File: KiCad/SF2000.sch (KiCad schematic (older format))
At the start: 71 parts, among them J1 Conn_2Rows-86Pins_even_odd, J2 Conn_01x02, J7 Conn_02x01, U1 LM1117-3.3, U19 74LVC1G57GV, U2 ABLIC S-1132B43-M5T1U, U3 TLV75533PDBVR, U4 SN74CBT16211, U5 SN74CBT16211, U6 SN74CBT3244PW, U7 SN74LVC16245ADGGR

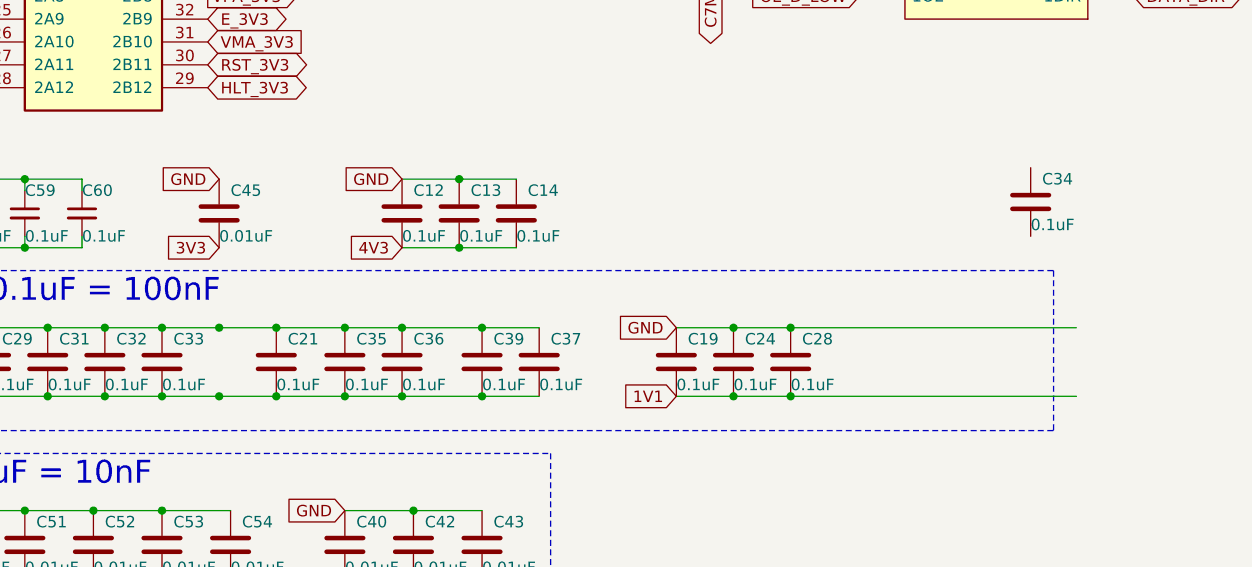
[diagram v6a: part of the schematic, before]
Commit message: Update C34,C35,C39 to 1206 4.7uF size and move to be used in RP2354A power circuit. Add a 33 Ohm series resistor on VREG_AVDD and use C34 for decoupling of the same.
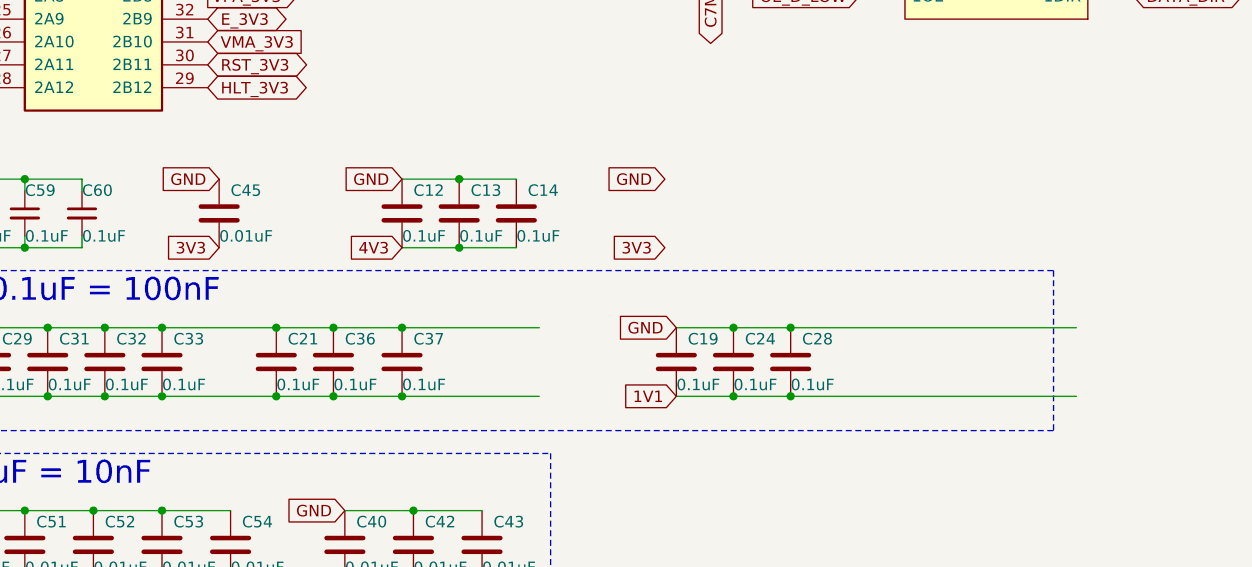
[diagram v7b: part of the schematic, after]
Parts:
- removed C34: 0.1uF, Capacitor_SMD:C_0805_2012Metric_Pad1.18x1.45mm_HandSolder, symbol Device:C
- removed C35, C39: 0.1uF, Capacitor_SMD:C_0805_2012Metric_Pad1.15x1.40mm_HandSolder, symbol Device:C
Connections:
- wire segments 135 -> 131
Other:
- moved on the sheet: C36, C37
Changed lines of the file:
@@
-$EndComp
-$Comp
-L Device:C C35
-U 1 1 62559B16
-P 6000 6150
-F 0 "C35" H 6050 6250 50  0000 L CNN
-F 1 "0.1uF" H 6000 6050 50  0000 L CNN
-F 2 "Capacitor_SMD:C_0805_2012Metric_Pad1.15x1.40mm_HandSolder" H 6038 6000 50  0001 C CNN
-F 3 "~" H 6000 6150 50  0001 C CNN
-	1    6000 6150
-	1    0    0    -1
 $EndComp
 $Comp
@@
 $EndComp
 $Comp
-L Device:C C39
-U 1 1 622B5AAE
-P 6600 6150
-F 0 "C39" H 6650 6250 50  0000 L CNN
-F 1 "0.1uF" H 6600 6050 50  0000 L CNN
-F 2 "Capacitor_SMD:C_0805_2012Metric_Pad1.15x1.40mm_HandSolder" H 6638 6000 50  0001 C CNN
-F 3 "~" H 6600 6150 50  0001 C CNN
-	1    6600 6150
-	1    0    0    -1
-$EndComp
-$Comp
 L Connector_Generic:Conn_02x01 J?
 U 1 1 62359ABC
@@
 $EndComp
 $Comp
-L Device:C C34
-U 1 1 68166D11
-P 9000 5450
-F 0 "C34" H 9050 5550 50  0000 L CNN
-F 1 "0.1uF" H 9000 5350 50  0000 L CNN
-F 2 "Capacitor_SMD:C_0805_2012Metric_Pad1.18x1.45mm_HandSolder" H 9038 5300 50  0001 C CNN
-F 3 "~" H 9000 5450 50  0001 C CNN
-	1    9000 5450
-	1    0    0    -1
-$EndComp
-$Comp
 L Device:C C33
 U 1 1 681A6453
@@
 L Device:C C37
 U 1 1 623F7CFB
-P 6850 6150
-F 0 "C37" H 6900 6250 50  0000 L CNN
-F 1 "0.1uF" H 6850 6050 50  0000 L CNN
-F 2 "Capacitor_SMD:C_0805_2012Metric_Pad1.15x1.40mm_HandSolder" H 6888 6000 50  0001 C CNN
-F 3 "~" H 6850 6150 50  0001 C CNN
-	1    6850 6150
+P 6250 6150
+F 0 "C37" H 6300 6250 50  0000 L CNN
+F 1 "0.1uF" H 6250 6050 50  0000 L CNN
+F 2 "Capacitor_SMD:C_0805_2012Metric_Pad1.15x1.40mm_HandSolder" H 6288 6000 50  0001 C CNN
+F 3 "~" H 6250 6150 50  0001 C CNN
+	1    6250 6150
 	1    0    0    -1
 $EndComp
@@
 L Device:C C36
 U 1 1 623F86B0
-P 6250 6150
-F 0 "C36" H 6300 6250 50  0000 L CNN
-F 1 "0.1uF" H 6250 6050 50  0000 L CNN
-F 2 "Capacitor_SMD:C_0805_2012Metric_Pad1.15x1.40mm_HandSolder" H 6288 6000 50  0001 C CNN
-F 3 "~" H 6250 6150 50  0001 C CNN
-	1    6250 6150
+P 5950 6150
+F 0 "C36" H 6000 6250 50  0000 L CNN
+F 1 "0.1uF" H 5950 6050 50  0000 L CNN
+F 2 "Capacitor_SMD:C_0805_2012Metric_Pad1.15x1.40mm_HandSolder" H 5988 6000 50  0001 C CNN
+F 3 "~" H 5950 6150 50  0001 C CNN
+	1    5950 6150
 	1    0    0    -1
 $EndComp
@@
 Wire Wire Line
 	2200 6050 2200 6000
-Wire Wire Line
-	5450 6000 5700 6000
-Connection ~ 5450 6000
 Connection ~ 5700 6000
-Wire Wire Line
-	5700 6000 6000 6000
-Wire Wire Line
-	5450 6300 5700 6300
-Connection ~ 5450 6300
 Connection ~ 5700 6300
-Wire Wire Line
-	5700 6300 6000 6300
 Wire Wire Line
 	7450 6000 7700 6000
@@
 Connection ~ 3950 6000
 Connection ~ 3950 6300
-Connection ~ 6000 6000
-Connection ~ 6000 6300
 Wire Wire Line
 	3950 6000 4200 6000
@@
 Wire Wire Line
 	4450 6300 4700 6300
-Wire Wire Line
-	6000 6000 6250 6000
-Wire Wire Line
-	6000 6300 6250 6300
 Connection ~ 6250 6000
-Wire Wire Line
-	6250 6000 6600 6000
 Connection ~ 6250 6300
-Wire Wire Line
-	6250 6300 6600 6300
 Connection ~ 4700 6000
 Connection ~ 4700 6300
 Wire Wire Line
-	6850 6000 6600 6000
-Wire Wire Line
 	4700 6000 4950 6000
 Wire Wire Line
 	4700 6300 4950 6300
-Connection ~ 6600 6000
-Wire Wire Line
-	6850 6300 6600 6300
-Connection ~ 6600 6300
 Connection ~ 4950 6000
 Wire Wire Line
@@
 	4950 6300 5200 6300
 Connection ~ 5200 6000
-Wire Wire Line
-	5200 6000 5450 6000
 Connection ~ 5200 6300
 Wire Wire Line
-	5200 6300 5450 6300
+	5200 6000 5700 6000
+Wire Wire Line
+	5200 6300 5700 6300
+Text GLabel 7400 5350 0    50   Input ~ 0
+GND
+Text GLabel 7400 5650 0    50   Input ~ 0
+3V3
+Wire Wire Line
+	5700 6000 5950 6000
+Wire Wire Line
+	5700 6300 5950 6300
+Wire Wire Line
+	6250 6000 6850 6000
+Wire Wire Line
+	6250 6300 6850 6300
+Connection ~ 5950 6000
+Wire Wire Line
+	5950 6000 6250 6000
+Connection ~ 5950 6300
+Wire Wire Line
+	5950 6300 6250 6300
 $EndSCHEMATC

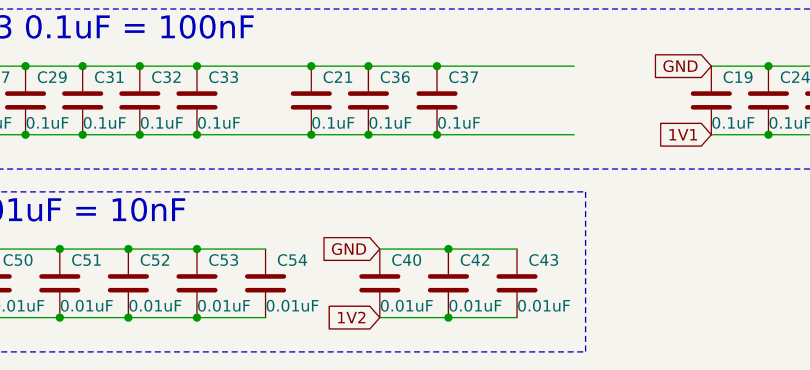
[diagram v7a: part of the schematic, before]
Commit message: Move C40 cap to RP2354A and the RESET-button circuit, change to 100nF value
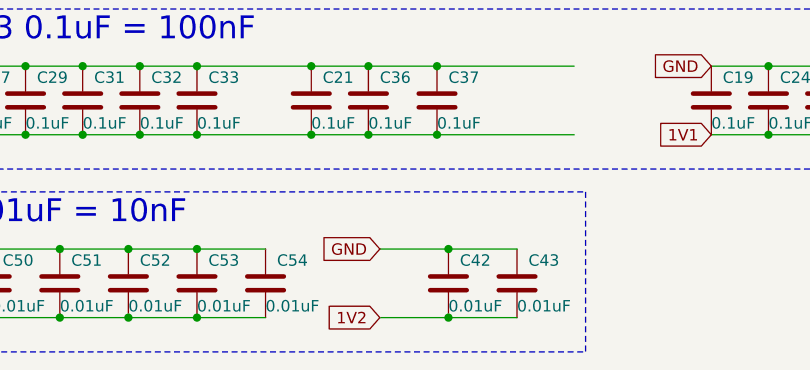
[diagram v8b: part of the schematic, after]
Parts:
- removed C40: 0.01uF, Capacitor_SMD:C_0805_2012Metric_Pad1.18x1.45mm_HandSolder, symbol Device:C
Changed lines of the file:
@@
 Wire Wire Line
 	6000 6800 6300 6800
-$Comp
-L Device:C C40
-U 1 1 6839385A
-P 6000 6950
-F 0 "C40" H 6050 7050 50  0000 L CNN
-F 1 "0.01uF" H 6000 6850 50  0000 L CNN
-F 2 "Capacitor_SMD:C_0805_2012Metric_Pad1.18x1.45mm_HandSolder" H 6038 6800 50  0001 C CNN
-F 3 "~" H 6000 6950 50  0001 C CNN
-	1    6000 6950
-	1    0    0    -1
-$EndComp
 Text GLabel 6000 6800 0    50   Input ~ 0
 GND
